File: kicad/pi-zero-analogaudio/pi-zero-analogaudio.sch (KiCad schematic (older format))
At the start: 9 parts, among them J1 AudioJack3

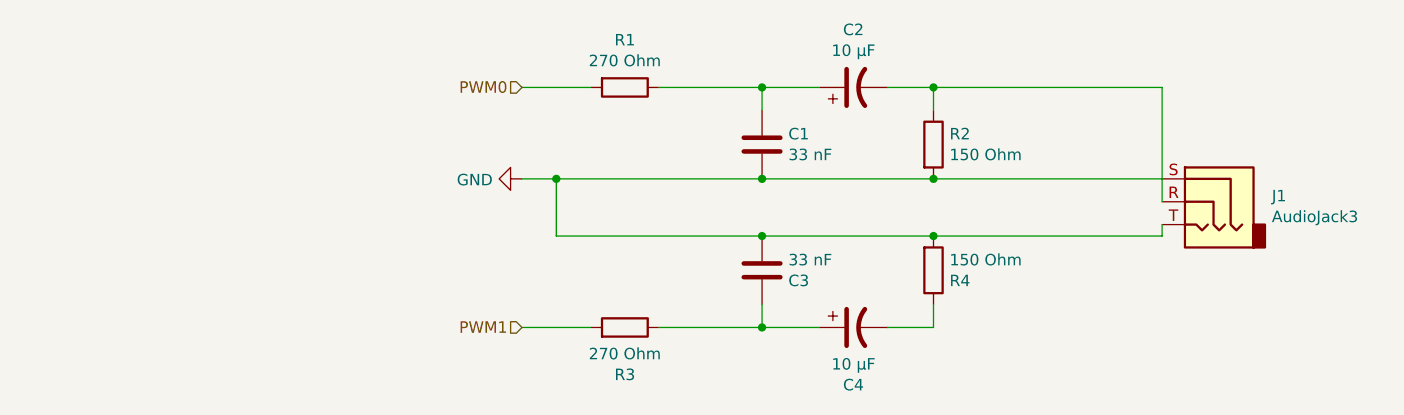
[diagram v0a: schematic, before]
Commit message: added 2x5 connector
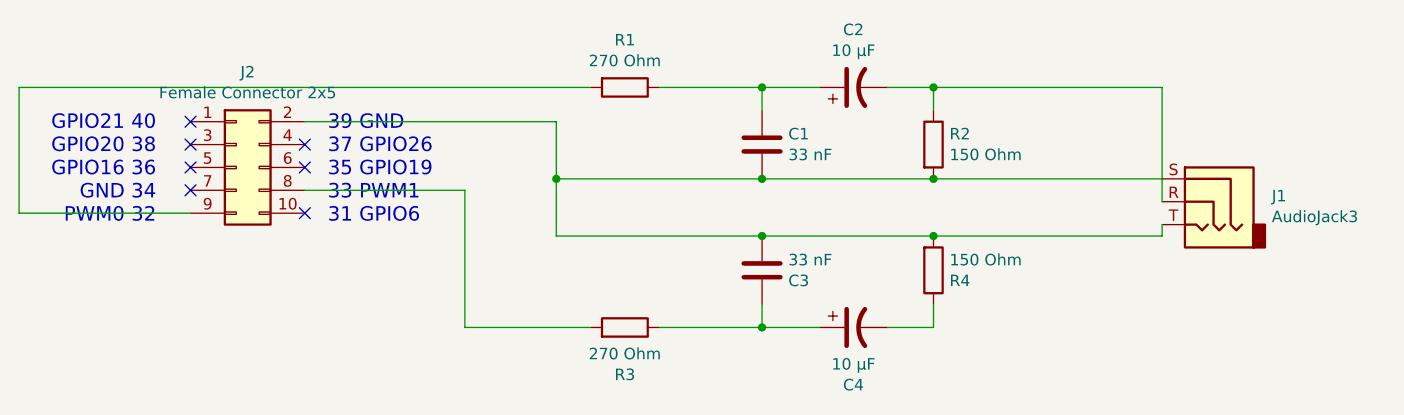
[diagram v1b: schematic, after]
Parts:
- added J2: Female Connector 2x5, symbol Connector_Generic:Conn_02x05_Odd_Even
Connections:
- net GND: no longer names the net of C1.2, C3.2, J1.S, J1.T, R2.2, R4.2
- net GND: now also J2.2 (Pin_2)
- net PWM0: no longer names the net of R1.2
- net PWM0: now also J2.9 (Pin_9)
- net PWM1: no longer names the net of R3.2
- net PWM1: now also J2.8 (Pin_8)
- no-connect marks 0 -> 7
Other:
- note added: "39 GND\n37 GPIO26\n35 GPIO19\n33 PWM1\n31 GPIO6\n"
- note added: "GPIO21 40\nGPIO20 38\nGPIO16 36\nGND 34\nPWM0 32"
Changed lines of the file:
@@
 Wire Wire Line
 	4850 1900 4100 1900
-$Comp
-L power:GND #PWR0101
-U 1 1 5DFFF61E
-P 3050 1900
-F 0 "#PWR0101" H 3050 1650 50  0001 C CNN
-F 1 "GND" V 3055 1772 50  0000 R CNN
-F 2 "" H 3050 1900 50  0001 C CNN
-F 3 "" H 3050 1900 50  0001 C CNN
-	1    3050 1900
-	0    1    1    0
-$EndComp
 Connection ~ 4100 1900
 $Comp
@@
 Wire Wire Line
 	3200 2150 3200 1900
-Wire Wire Line
-	3050 1900 3200 1900
-Connection ~ 3200 1900
 $Comp
 L Connector:AudioJack3 J1
@@
 	-1   0    0    -1
 $EndComp
-Text HLabel 3050 1500 0    50   Input ~ 0
-PWM0
-Text HLabel 3050 2550 0    50   Input ~ 0
-PWM1
-Wire Wire Line
-	3350 1500 3050 1500
-Wire Wire Line
-	3350 2550 3050 2550
 Wire Wire Line
 	4850 1900 5850 1900
@@
 Wire Wire Line
 	5850 1500 5850 2000
+$Comp
+L Connector_Generic:Conn_02x05_Odd_Even J2
+U 1 1 5E0099F7
+P 1800 1850
+F 0 "J2" H 1850 2267 50  0000 C CNN
+F 1 "Female Connector 2x5" H 1850 2176 50  0000 C CNN
+F 2 "" H 1800 1850 50  0001 C CNN
+F 3 "~" H 1800 1850 50  0001 C CNN
+	1    1800 1850
+	1    0    0    -1
+$EndComp
+Text Notes 1450 2100 2    63   ~ 0
+GPIO21 40\nGPIO20 38\nGPIO16 36\nGND 34\nPWM0 32
+Text Notes 2200 2100 0    63   ~ 0
+39 GND\n37 GPIO26\n35 GPIO19\n33 PWM1\n31 GPIO6\n
+Wire Wire Line
+	3200 1900 3200 1650
+Wire Wire Line
+	3200 1650 2100 1650
+Connection ~ 3200 1900
+Wire Wire Line
+	3350 2550 2800 2550
+Wire Wire Line
+	2800 2550 2800 1950
+Wire Wire Line
+	2800 1950 2100 1950
+Wire Wire Line
+	3350 1500 850  1500
+Wire Wire Line
+	850  1500 850  2050
+Wire Wire Line
+	850  2050 1600 2050
+NoConn ~ 1600 1650
+NoConn ~ 1600 1750
+NoConn ~ 1600 1850
+NoConn ~ 1600 1950
+NoConn ~ 2100 1750
+NoConn ~ 2100 1850
+NoConn ~ 2100 2050
 $EndSCHEMATC
